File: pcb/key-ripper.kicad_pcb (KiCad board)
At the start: 2 copper layers, 285.8 x 116.7 mm, 193 parts, among them J1 Conn_01x04, SW1 ESC, SW10 F9, SW11 F10, SW12 F11, SW13 F12, SW14 TILDE, SW15 1, SW16 2, SW17 3, SW18 4, SW19 5, SW2 F1, SW20 6, SW21 7, SW22 8, SW23 9, SW24 0, SW25 -, SW26 +, SW27 BACKSPACE, SW28 TAB, SW29 Q, SW3 F2, SW30 W, SW31 E, SW32 R, SW33 T, SW34 Y, SW35 U, SW36 I, SW37 O, SW38 P, SW39 [, SW4 F3, SW40 ], SW41 BACKSLASH, SW42 CAPS, SW43 A, SW44 S, SW45 D, SW46 F, SW47 G, SW48 H, SW49 J, SW5 F4, SW50 K, SW51 L, SW52 ;, SW53 ', SW54 ENTER, SW55 L_SHIFT, SW56 Z, SW57 X, SW58 C, SW59 V, SW6 F5, SW60 B, SW61 N, SW62 M, SW63 ,, SW64 ., SW65 FWD_SLASH, SW66 UP, SW67 FN, SW68 BL_CTRL, SW69 L_ALT, SW7 F6, SW70 L_CMD, SW71 SPACE, SW72 R_CMD, SW73 LEFT, SW74 DOWN, SW75 RIGHT, SW8 F7, SW9 F8, U1 RP2040, U2 TYPE-C-31-M-12, U3 XC6206PxxxMR, U4 W25Q128JVS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

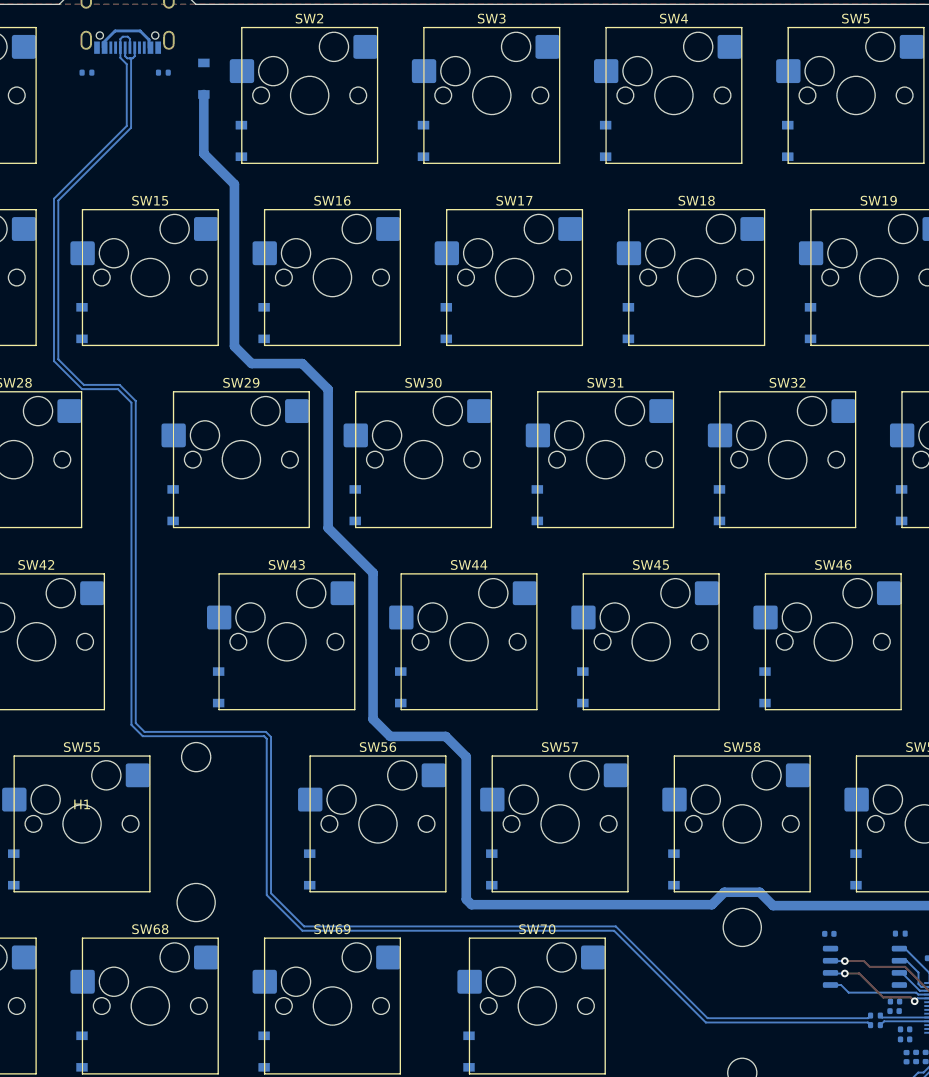
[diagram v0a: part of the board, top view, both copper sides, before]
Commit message: Tune the skew of the USB differential pair
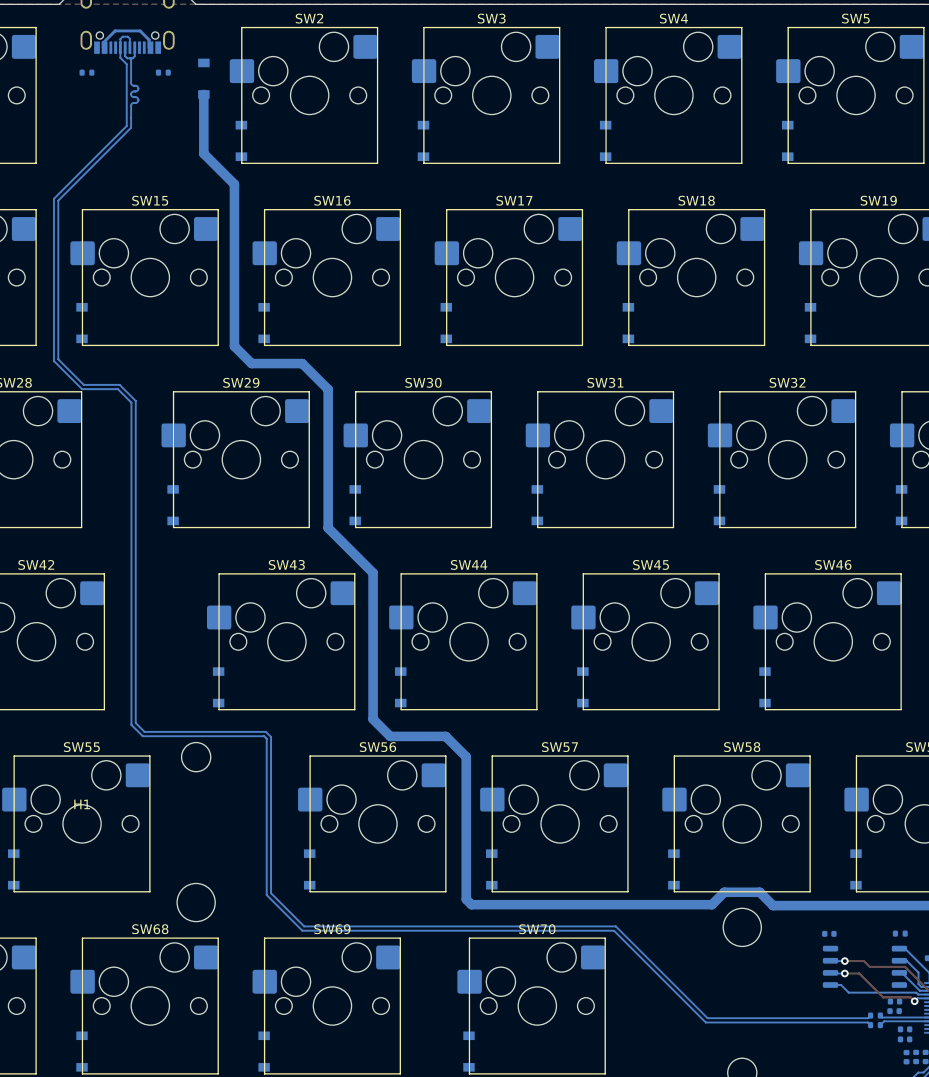
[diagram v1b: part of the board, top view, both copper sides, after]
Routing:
- net USB+: track 180.7 -> 182.6 mm
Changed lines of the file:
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@@
   (segment (start 18.91767 -24.86358) (end 18.91767 -24.047163) (width 0.3) (layer "B.Cu") (net 94))
   (segment (start 17.417797 -23.148268) (end 17.200779 -22.93125) (width 0.2) (layer "B.Cu") (net 100))
-  (segment (start 94.39 77.2) (end 94.115001 77.474999) (width 0.2) (layer "B.Cu") (net 100))
-  (segment (start 18.4432 47.525) (end 17.525 46.6068) (width 0.2) (layer "B.Cu") (net 100))
-  (segment (start 17.035009 -15.666809) (end 17.035009 -22.864991) (width 0.2) (layer "B.Cu") (net 100))
-  (segment (start 94.115001 77.474999) (end 77.343199 77.474999) (width 0.2) (layer "B.Cu") (net 100))
-  (segment (start 31.675 48.0568) (end 31.1432 47.525) (width 0.2) (layer "B.Cu") (net 100))
-  (segment (start 17.525 12.9068) (end 15.8432 11.225) (width 0.2) (layer "B.Cu") (net 100))
-  (segment (start 35.1432 67.875) (end 31.675 64.4068) (width 0.2) (layer "B.Cu") (net 100))
-  (segment (start 17.035009 -22.864991) (end 16.96875 -22.93125) (width 0.2) (layer "B.Cu") (net 100))
+  (segment (start 17.502979 -18.264991) (end 17.335009 -18.264991) (width 0.2) (layer "B.Cu") (net 100))
+  (segment (start 17.525 46.6068) (end 18.4432 47.525) (width 0.2) (layer "B.Cu") (net 100))
+  (segment (start 17.502979 -19.464991) (end 17.335009 -19.464991) (width 0.2) (layer "B.Cu") (net 100))
+  (segment (start 31.1432 47.525) (end 31.675 48.0568) (width 0.2) (layer "B.Cu") (net 100))
+  (segment (start 17.035009 -15.666809) (end 9.425 -8.0568) (width 0.2) (layer "B.Cu") (net 100))
+  (segment (start 15.8432 11.225) (end 17.525 12.9068) (width 0.2) (layer "B.Cu") (net 100))
+  (segment (start 67.7432 67.875) (end 77.343199 77.474999) (width 0.2) (layer "B.Cu") (net 100))
+  (segment (start 94.115001 77.474999) (end 94.39 77.2) (width 0.2) (layer "B.Cu") (net 100))
   (segment (start 17.200779 -22.93125) (end 16.9 -22.93125) (width 0.2) (layer "B.Cu") (net 100))
-  (segment (start 9.425 -8.0568) (end 17.035009 -15.666809) (width 0.2) (layer "B.Cu") (net 100))
-  (segment (start 9.425 8.5568) (end 9.425 -8.0568) (width 0.2) (layer "B.Cu") (net 100))
-  (segment (start 17.525 46.6068) (end 17.525 12.9068) (width 0.2) (layer "B.Cu") (net 100))
-  (segment (start 77.343199 77.474999) (end 67.7432 67.875) (width 0.2) (layer "B.Cu") (net 100))
-  (segment (start 31.675 64.4068) (end 31.675 48.0568) (width 0.2) (layer "B.Cu") (net 100))
+  (segment (start 16.96875 -22.93125) (end 17.035009 -22.864991) (width 0.2) (layer "B.Cu") (net 100))
+  (segment (start 17.035009 -17.964991) (end 17.035009 -16.714991) (width 0.2) (layer "B.Cu") (net 100))
+  (segment (start 31.675 48.0568) (end 31.675 64.4068) (width 0.2) (layer "B.Cu") (net 100))
   (segment (start 16.417797 -23.148014) (end 16.417797 -24.047163) (width 0.2) (layer "B.Cu") (net 100))
-  (segment (start 12.0932 11.225) (end 9.425 8.5568) (width 0.2) (layer "B.Cu") (net 100))
-  (segment (start 15.8432 11.225) (end 12.0932 11.225) (width 0.2) (layer "B.Cu") (net 100))
+  (segment (start 17.335009 -18.864991) (end 17.502979 -18.864991) (width 0.2) (layer "B.Cu") (net 100))
   (segment (start 16.9 -22.93125) (end 16.634561 -22.93125) (width 0.2) (layer "B.Cu") (net 100))
-  (segment (start 67.7432 67.875) (end 35.1432 67.875) (width 0.2) (layer "B.Cu") (net 100))
-  (segment (start 16.96875 -22.93125) (end 16.9 -22.93125) (width 0.2) (layer "B.Cu") (net 100))
-  (segment (start 31.1432 47.525) (end 18.4432 47.525) (width 0.2) (layer "B.Cu") (net 100))
+  (segment (start 35.1432 67.875) (end 67.7432 67.875) (width 0.2) (layer "B.Cu") (net 100))
+  (segment (start 17.335009 -20.064991) (end 17.502979 -20.064991) (width 0.2) (layer "B.Cu") (net 100))
+  (segment (start 9.425 8.5568) (end 12.0932 11.225) (width 0.2) (layer "B.Cu") (net 100))
+  (segment (start 31.675 64.4068) (end 35.1432 67.875) (width 0.2) (layer "B.Cu") (net 100))
+  (segment (start 17.525 12.9068) (end 17.525 46.6068) (width 0.2) (layer "B.Cu") (net 100))
+  (segment (start 9.425 -8.0568) (end 9.425 8.5568) (width 0.2) (layer "B.Cu") (net 100))
+  (segment (start 17.035009 -22.864991) (end 17.035009 -20.364991) (width 0.2) (layer "B.Cu") (net 100))
+  (segment (start 17.035009 -16.714991) (end 17.035009 -15.666809) (width 0.2) (layer "B.Cu") (net 100))
+  (segment (start 12.0932 11.225) (end 15.8432 11.225) (width 0.2) (layer "B.Cu") (net 100))
+  (segment (start 18.4432 47.525) (end 31.1432 47.525) (width 0.2) (layer "B.Cu") (net 100))
+  (segment (start 16.9 -22.93125) (end 16.96875 -22.93125) (width 0.2) (layer "B.Cu") (net 100))
   (segment (start 16.634561 -22.93125) (end 16.417797 -23.148014) (width 0.2) (layer "B.Cu") (net 100))
+  (segment (start 77.343199 77.474999) (end 94.115001 77.474999) (width 0.2) (layer "B.Cu") (net 100))
   (segment (start 17.417797 -24.047163) (end 17.417797 -23.148268) (width 0.2) (layer "B.Cu") (net 100))
+  (arc (start 17.502979 -20.064991) (mid 17.715111 -19.977123) (end 17.802979 -19.764991) (width 0.2) (layer "B.Cu") (net 100))
+  (arc (start 17.502979 -18.864991) (mid 17.715111 -18.777123) (end 17.802979 -18.564991) (width 0.2) (layer "B.Cu") (net 100))
+  (arc (start 17.335009 -18.264991) (mid 17.122877 -18.177123) (end 17.035009 -17.964991) (width 0.2) (layer "B.Cu") (net 100))
+  (arc (start 17.035009 -19.164991) (mid 17.122877 -18.952859) (end 17.335009 -18.864991) (width 0.2) (layer "B.Cu") (net 100))
+  (arc (start 17.802979 -19.764991) (mid 17.715111 -19.552859) (end 17.502979 -19.464991) (width 0.2) (layer "B.Cu") (net 100))
+  (arc (start 17.802979 -18.564991) (mid 17.715111 -18.352859) (end 17.502979 -18.264991) (width 0.2) (layer "B.Cu") (net 100))
+  (arc (start 17.335009 -19.464991) (mid 17.122877 -19.377123) (end 17.035009 -19.164991) (width 0.2) (layer "B.Cu") (net 100))
+  (arc (start 17.035009 -20.364991) (mid 17.122877 -20.152859) (end 17.335009 -20.064991) (width 0.2) (layer "B.Cu") (net 100))
+  (segment (start 11.9068 11.675) (end 8.975 8.7432) (width 0.2) (layer "B.Cu") (net 101))
+  (segment (start 77.156801 77.925001) (end 67.5568 68.325) (width 0.2) (layer "B.Cu") (net 101))
   (segment (start 16.6875 -25.19375) (end 16.91767 -24.96358) (width 0.2) (layer "B.Cu") (net 101))
   (segment (start 16.165362 -25.19375) (end 16.6875 -25.19375) (width 0.2) (layer "B.Cu") (net 101))
-  (segment (start 16.585009 -22.314991) (end 15.91767 -22.98233) (width 0.2) (layer "B.Cu") (net 101))
-  (segment (start 94.115001 77.925001) (end 77.156801 77.925001) (width 0.2) (layer "B.Cu") (net 101))
+  (segment (start 8.975 8.7432) (end 8.975 -8.2432) (width 0.2) (layer "B.Cu") (net 101))
+  (segment (start 34.9568 68.325) (end 31.225 64.5932) (width 0.2) (layer "B.Cu") (net 101))
   (segment (start 16.91767 -24.96358) (end 16.91767 -24.047163) (width 0.2) (layer "B.Cu") (net 101))
+  (segment (start 16.585009 -15.853209) (end 16.585009 -22.314991) (width 0.2) (layer "B.Cu") (net 101))
+  (segment (start 31.225 48.2432) (end 30.9568 47.975) (width 0.2) (layer "B.Cu") (net 101))
+  (segment (start 15.91767 -22.98233) (end 15.91767 -24.047163) (width 0.2) (layer "B.Cu") (net 101))
   (segment (start 94.39 78.2) (end 94.115001 77.925001) (width 0.2) (layer "B.Cu") (net 101))
+  (segment (start 17.075 46.7932) (end 17.075 13.0932) (width 0.2) (layer "B.Cu") (net 101))
+  (segment (start 15.6568 11.675) (end 11.9068 11.675) (width 0.2) (layer "B.Cu") (net 101))
+  (segment (start 30.9568 47.975) (end 18.2568 47.975) (width 0.2) (layer "B.Cu") (net 101))
   (segment (start 18.2568 47.975) (end 17.075 46.7932) (width 0.2) (layer "B.Cu") (net 101))
   (segment (start 15.91767 -24.946058) (end 16.165362 -25.19375) (width 0.2) (layer "B.Cu") (net 101))
+  (segment (start 17.075 13.0932) (end 15.6568 11.675) (width 0.2) (layer "B.Cu") (net 101))
+  (segment (start 16.585009 -22.314991) (end 15.91767 -22.98233) (width 0.2) (layer "B.Cu") (net 101))
   (segment (start 8.975 -8.2432) (end 16.585009 -15.853209) (width 0.2) (layer "B.Cu") (net 101))
-  (segment (start 15.6568 11.675) (end 11.9068 11.675) (width 0.2) (layer "B.Cu") (net 101))
-  (segment (start 16.585009 -15.853209) (end 16.585009 -22.314991) (width 0.2) (layer "B.Cu") (net 101))
+  (segment (start 94.115001 77.925001) (end 77.156801 77.925001) (width 0.2) (layer "B.Cu") (net 101))
+  (segment (start 15.91767 -24.047163) (end 15.91767 -24.946058) (width 0.2) (layer "B.Cu") (net 101))
   (segment (start 67.5568 68.325) (end 34.9568 68.325) (width 0.2) (layer "B.Cu") (net 101))
-  (segment (start 17.075 46.7932) (end 17.075 13.0932) (width 0.2) (layer "B.Cu") (net 101))
-  (segment (start 17.075 13.0932) (end 15.6568 11.675) (width 0.2) (layer "B.Cu") (net 101))
   (segment (start 31.225 64.5932) (end 31.225 48.2432) (width 0.2) (layer "B.Cu") (net 101))
-  (segment (start 34.9568 68.325) (end 31.225 64.5932) (width 0.2) (layer "B.Cu") (net 101))
-  (segment (start 77.156801 77.925001) (end 67.5568 68.325) (width 0.2) (layer "B.Cu") (net 101))
-  (segment (start 15.91767 -24.047163) (end 15.91767 -24.946058) (width 0.2) (layer "B.Cu") (net 101))
-  (segment (start 31.225 48.2432) (end 30.9568 47.975) (width 0.2) (layer "B.Cu") (net 101))
-  (segment (start 11.9068 11.675) (end 8.975 8.7432) (width 0.2) (layer "B.Cu") (net 101))
-  (segment (start 30.9568 47.975) (end 18.2568 47.975) (width 0.2) (layer "B.Cu") (net 101))
-  (segment (start 8.975 8.7432) (end 8.975 -8.2432) (width 0.2) (layer "B.Cu") (net 101))
-  (segment (start 15.91767 -22.98233) (end 15.91767 -24.047163) (width 0.2) (layer "B.Cu") (net 101))
   (segment (start 100.549962 73.800051) (end 100.099962 73.800051) (width 0.2) (layer "B.Cu") (net 102))
   (segment (start 100.549962 73.800051) (end 100.549962 72.749962) (width 0.2) (layer "B.Cu") (net 102))

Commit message: Undo skew tuning, probably not needed for now
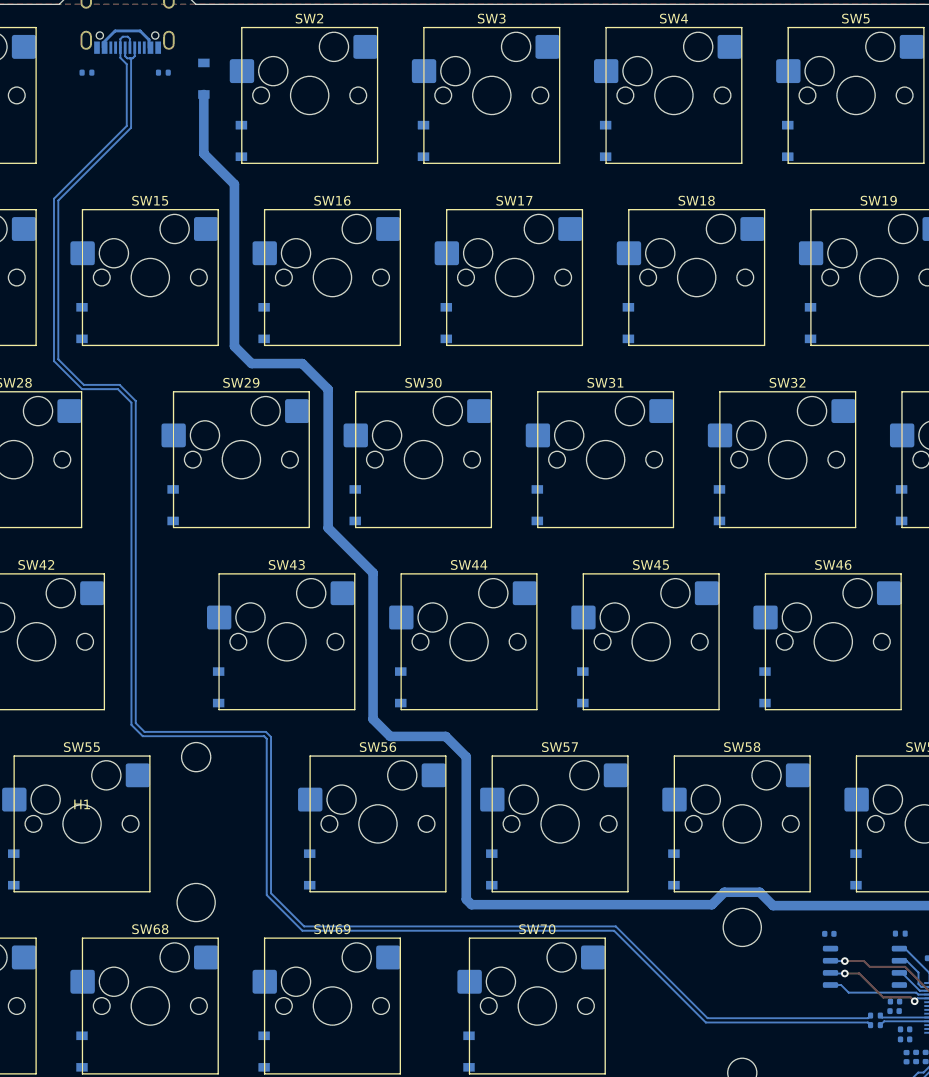
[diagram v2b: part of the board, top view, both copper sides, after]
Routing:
- net USB+: track 182.6 -> 180.7 mm
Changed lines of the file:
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@@
   (segment (start 18.91767 -24.86358) (end 18.91767 -24.047163) (width 0.3) (layer "B.Cu") (net 94))
   (segment (start 17.417797 -23.148268) (end 17.200779 -22.93125) (width 0.2) (layer "B.Cu") (net 100))
-  (segment (start 17.502979 -18.264991) (end 17.335009 -18.264991) (width 0.2) (layer "B.Cu") (net 100))
-  (segment (start 17.525 46.6068) (end 18.4432 47.525) (width 0.2) (layer "B.Cu") (net 100))
-  (segment (start 17.502979 -19.464991) (end 17.335009 -19.464991) (width 0.2) (layer "B.Cu") (net 100))
-  (segment (start 31.1432 47.525) (end 31.675 48.0568) (width 0.2) (layer "B.Cu") (net 100))
-  (segment (start 17.035009 -15.666809) (end 9.425 -8.0568) (width 0.2) (layer "B.Cu") (net 100))
-  (segment (start 15.8432 11.225) (end 17.525 12.9068) (width 0.2) (layer "B.Cu") (net 100))
-  (segment (start 67.7432 67.875) (end 77.343199 77.474999) (width 0.2) (layer "B.Cu") (net 100))
-  (segment (start 94.115001 77.474999) (end 94.39 77.2) (width 0.2) (layer "B.Cu") (net 100))
+  (segment (start 94.39 77.2) (end 94.115001 77.474999) (width 0.2) (layer "B.Cu") (net 100))
+  (segment (start 18.4432 47.525) (end 17.525 46.6068) (width 0.2) (layer "B.Cu") (net 100))
+  (segment (start 17.035009 -15.666809) (end 17.035009 -22.864991) (width 0.2) (layer "B.Cu") (net 100))
+  (segment (start 94.115001 77.474999) (end 77.343199 77.474999) (width 0.2) (layer "B.Cu") (net 100))
+  (segment (start 31.675 48.0568) (end 31.1432 47.525) (width 0.2) (layer "B.Cu") (net 100))
+  (segment (start 17.525 12.9068) (end 15.8432 11.225) (width 0.2) (layer "B.Cu") (net 100))
+  (segment (start 35.1432 67.875) (end 31.675 64.4068) (width 0.2) (layer "B.Cu") (net 100))
+  (segment (start 17.035009 -22.864991) (end 16.96875 -22.93125) (width 0.2) (layer "B.Cu") (net 100))
   (segment (start 17.200779 -22.93125) (end 16.9 -22.93125) (width 0.2) (layer "B.Cu") (net 100))
-  (segment (start 16.96875 -22.93125) (end 17.035009 -22.864991) (width 0.2) (layer "B.Cu") (net 100))
-  (segment (start 17.035009 -17.964991) (end 17.035009 -16.714991) (width 0.2) (layer "B.Cu") (net 100))
-  (segment (start 31.675 48.0568) (end 31.675 64.4068) (width 0.2) (layer "B.Cu") (net 100))
+  (segment (start 9.425 -8.0568) (end 17.035009 -15.666809) (width 0.2) (layer "B.Cu") (net 100))
+  (segment (start 9.425 8.5568) (end 9.425 -8.0568) (width 0.2) (layer "B.Cu") (net 100))
+  (segment (start 17.525 46.6068) (end 17.525 12.9068) (width 0.2) (layer "B.Cu") (net 100))
+  (segment (start 77.343199 77.474999) (end 67.7432 67.875) (width 0.2) (layer "B.Cu") (net 100))
+  (segment (start 31.675 64.4068) (end 31.675 48.0568) (width 0.2) (layer "B.Cu") (net 100))
   (segment (start 16.417797 -23.148014) (end 16.417797 -24.047163) (width 0.2) (layer "B.Cu") (net 100))
-  (segment (start 17.335009 -18.864991) (end 17.502979 -18.864991) (width 0.2) (layer "B.Cu") (net 100))
+  (segment (start 12.0932 11.225) (end 9.425 8.5568) (width 0.2) (layer "B.Cu") (net 100))
+  (segment (start 15.8432 11.225) (end 12.0932 11.225) (width 0.2) (layer "B.Cu") (net 100))
   (segment (start 16.9 -22.93125) (end 16.634561 -22.93125) (width 0.2) (layer "B.Cu") (net 100))
-  (segment (start 35.1432 67.875) (end 67.7432 67.875) (width 0.2) (layer "B.Cu") (net 100))
-  (segment (start 17.335009 -20.064991) (end 17.502979 -20.064991) (width 0.2) (layer "B.Cu") (net 100))
-  (segment (start 9.425 8.5568) (end 12.0932 11.225) (width 0.2) (layer "B.Cu") (net 100))
-  (segment (start 31.675 64.4068) (end 35.1432 67.875) (width 0.2) (layer "B.Cu") (net 100))
-  (segment (start 17.525 12.9068) (end 17.525 46.6068) (width 0.2) (layer "B.Cu") (net 100))
-  (segment (start 9.425 -8.0568) (end 9.425 8.5568) (width 0.2) (layer "B.Cu") (net 100))
-  (segment (start 17.035009 -22.864991) (end 17.035009 -20.364991) (width 0.2) (layer "B.Cu") (net 100))
-  (segment (start 17.035009 -16.714991) (end 17.035009 -15.666809) (width 0.2) (layer "B.Cu") (net 100))
-  (segment (start 12.0932 11.225) (end 15.8432 11.225) (width 0.2) (layer "B.Cu") (net 100))
-  (segment (start 18.4432 47.525) (end 31.1432 47.525) (width 0.2) (layer "B.Cu") (net 100))
-  (segment (start 16.9 -22.93125) (end 16.96875 -22.93125) (width 0.2) (layer "B.Cu") (net 100))
+  (segment (start 67.7432 67.875) (end 35.1432 67.875) (width 0.2) (layer "B.Cu") (net 100))
+  (segment (start 16.96875 -22.93125) (end 16.9 -22.93125) (width 0.2) (layer "B.Cu") (net 100))
+  (segment (start 31.1432 47.525) (end 18.4432 47.525) (width 0.2) (layer "B.Cu") (net 100))
   (segment (start 16.634561 -22.93125) (end 16.417797 -23.148014) (width 0.2) (layer "B.Cu") (net 100))
-  (segment (start 77.343199 77.474999) (end 94.115001 77.474999) (width 0.2) (layer "B.Cu") (net 100))
   (segment (start 17.417797 -24.047163) (end 17.417797 -23.148268) (width 0.2) (layer "B.Cu") (net 100))
-  (arc (start 17.502979 -20.064991) (mid 17.715111 -19.977123) (end 17.802979 -19.764991) (width 0.2) (layer "B.Cu") (net 100))
-  (arc (start 17.502979 -18.864991) (mid 17.715111 -18.777123) (end 17.802979 -18.564991) (width 0.2) (layer "B.Cu") (net 100))
-  (arc (start 17.335009 -18.264991) (mid 17.122877 -18.177123) (end 17.035009 -17.964991) (width 0.2) (layer "B.Cu") (net 100))
-  (arc (start 17.035009 -19.164991) (mid 17.122877 -18.952859) (end 17.335009 -18.864991) (width 0.2) (layer "B.Cu") (net 100))
-  (arc (start 17.802979 -19.764991) (mid 17.715111 -19.552859) (end 17.502979 -19.464991) (width 0.2) (layer "B.Cu") (net 100))
-  (arc (start 17.802979 -18.564991) (mid 17.715111 -18.352859) (end 17.502979 -18.264991) (width 0.2) (layer "B.Cu") (net 100))
-  (arc (start 17.335009 -19.464991) (mid 17.122877 -19.377123) (end 17.035009 -19.164991) (width 0.2) (layer "B.Cu") (net 100))
-  (arc (start 17.035009 -20.364991) (mid 17.122877 -20.152859) (end 17.335009 -20.064991) (width 0.2) (layer "B.Cu") (net 100))
   (segment (start 11.9068 11.675) (end 8.975 8.7432) (width 0.2) (layer "B.Cu") (net 101))
   (segment (start 77.156801 77.925001) (end 67.5568 68.325) (width 0.2) (layer "B.Cu") (net 101))
